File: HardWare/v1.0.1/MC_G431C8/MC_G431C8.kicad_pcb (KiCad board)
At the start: 2 copper layers, 154 parts, among them J1 Conn_01x02, J2 Conn_01x03, J3 Conn_01x04, J4 Conn_01x06, J5 Conn_01x03, Q1 MMBT3904L, U1 STM32G431C8, U2 fd6288t, U3 LMV324I, U4 TL431DBZ, U5 SGM6232YPS8G, U6 AMS1117-3.3, U7 AMS1117-5.0, U8 AS5047D, Y1 32MHZ

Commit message: 20240605 01:28 完成硬件初步布局
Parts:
- C12, C13, C26, C27, C28, C29, C30, C31, C5, C6, C8, C9, D10, D11, D12, D13, D4, D8, D9, R19, R2, R20, R21, R22, R24, R25, R26, R27, R30, R31, R32, R33, R7, TP1, TP10, TP11, TP12, TP13, TP14, TP15, TP16, TP17, TP18, TP19, TP2, TP4, TP5, TP6, TP7, TP8, TP9: moved to B.Cu
- moved U3 151.7 mm to (167.6, 105.4)
- moved U8 148.9 mm to (188.0, 85.1)
- moved Q8 126.9 mm to (165.4, 80.8), turned to 90 degrees
- moved Q6 122.0 mm to (158.7, 80.8), turned to 90 degrees
- moved R29 119.1 mm to (176.5, 108.0), turned to 180 degrees
- moved C36 115.9 mm to (166.6, 95.4)
- moved C37 115.9 mm to (166.6, 97.9)
- moved C38 115.9 mm to (166.6, 100.4)
- moved R35 115.9 mm to (174.6, 97.9)
- moved R36 115.9 mm to (174.6, 100.4)
- moved R37 115.9 mm to (174.6, 102.9)
- moved R38 115.9 mm to (174.6, 105.4)
- moved R42 115.9 mm to (178.6, 95.4)
- moved R43 115.9 mm to (178.6, 97.9)
- moved R44 115.9 mm to (178.6, 100.4)
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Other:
- board outline added: 100 x 50 mm

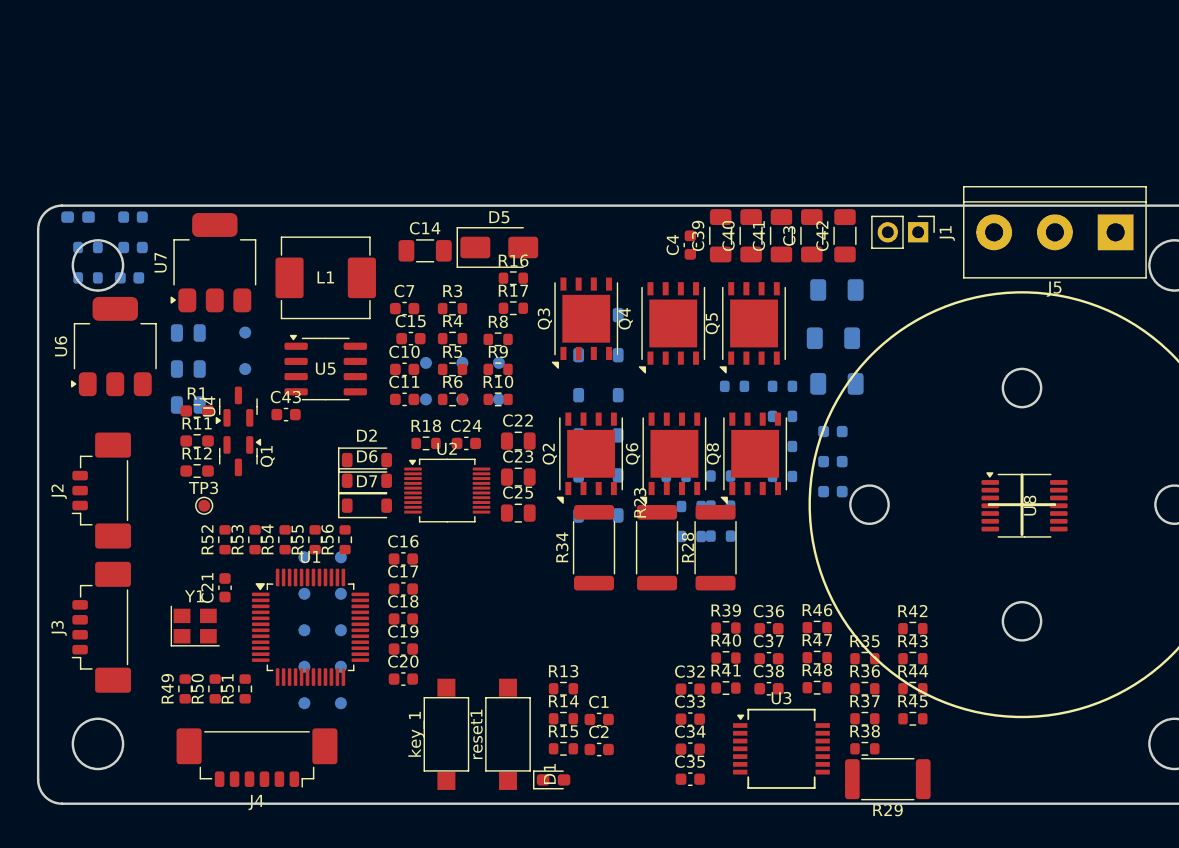
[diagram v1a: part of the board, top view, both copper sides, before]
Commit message: 20240606 01:01 硬件:电源布局完成
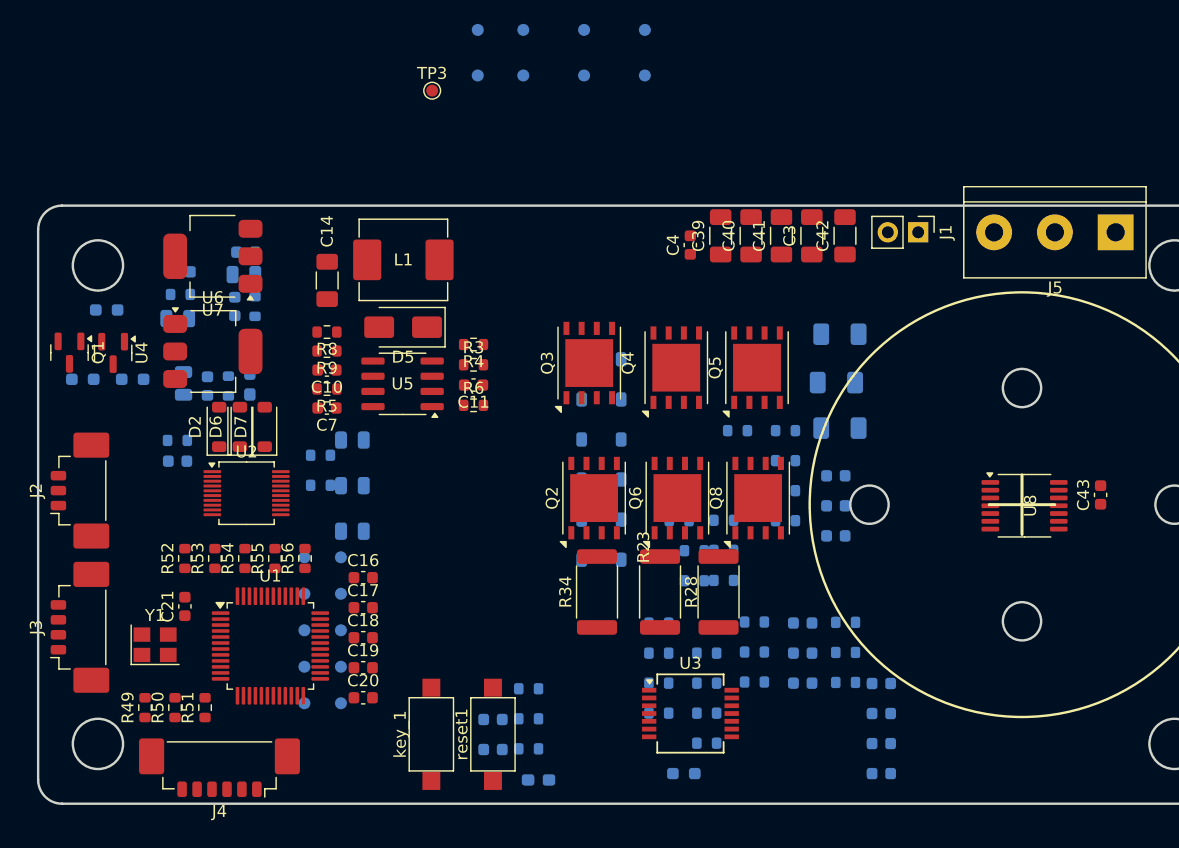
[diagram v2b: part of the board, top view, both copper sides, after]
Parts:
- C1, C15, C2, C22, C23, C24, C25, C32, C33, C34, C35, C36, C37, C38, D1, R1, R10, R11, R12, R13, R14, R15, R16, R17, R18, R35, R36, R37, R38, R39, R40, R41, R42, R43, R44, R45, R46, R47, R48: moved to B.Cu
- R29: footprint Resistor_SMD:R_2512_6332Metric -> Resistor_SMD:R_0603_1608Metric_Pad0.98x0.95mm_HandSolder; moved to B.Cu
- moved C43 68.4 mm to (194.3, 84.2), turned to 90 degrees
- moved TP3 39.6 mm to (138.4, 50.4)
- moved TP2 34.4 mm to (142.2, 45.3)
- moved TP16 31.7 mm to (156.2, 45.3)
- moved TP15 29.7 mm to (156.2, 49.1)
- moved TP18 29.0 mm to (146.1, 45.3)
- moved TP1 29.0 mm to (142.2, 49.1)
- moved TP17 28.9 mm to (151.1, 49.1)
- moved TP14 28.7 mm to (151.1, 45.3)
- moved TP19 28.3 mm to (146.1, 49.1)
- moved C24 24.2 mm to (117.2, 81.4), turned to 180 degrees
- moved R16 21.9 mm to (129.1, 80.9), turned to 180 degrees
- moved R17 21.9 mm to (129.1, 83.4), turned to 180 degrees
- moved R10 21.8 mm to (123.6, 68.4), turned to 90 degrees
- moved R42 21.2 mm to (157.4, 94.9), turned to 180 degrees
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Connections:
- TP11 pad 1: /TIM1_CH1N -> unconnected-(TP11-Pad1)

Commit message: 20240607 01:44 硬件初步布局已完成
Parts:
- C16, C17, C18, C19, R49, R50, R51, R52, R53, R54, R55, R56, TP3: moved to B.Cu
- R21, R22, R26, R27, R32, R33: moved to F.Cu
- moved TP18 82.6 mm to (69.4, 76.0)
- moved TP19 82.6 mm to (69.4, 79.9)
- moved TP1 82.6 mm to (65.5, 79.9)
- moved TP15 82.6 mm to (79.5, 79.9)
- moved TP16 82.6 mm to (79.5, 76.0)
- moved TP2 82.6 mm to (65.5, 76.0)
- moved TP14 82.6 mm to (74.4, 76.0)
- moved TP17 82.6 mm to (74.4, 79.9)
- moved TP3 64.2 mm to (81.5, 80.1), turned to 180 degrees
- moved TP4 47.6 mm to (85.1, 76.0), turned to -90 degrees
- moved TP5 45.7 mm to (88.1, 76.0), turned to -90 degrees
- moved TP6 44.1 mm to (91.2, 76.0), turned to -90 degrees
- moved TP9 43.9 mm to (85.1, 79.1), turned to -90 degrees
- moved TP7 42.9 mm to (94.2, 76.0), turned to -90 degrees
- moved C34 42.6 mm to (133.4, 103.7), turned to 90 degrees
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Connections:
- C20 pad 2: Net-(C20-Pad2) -> GND
- C21 pad 2: Net-(C20-Pad2) -> GND
- R51 pad 1: /SPI1_CS -> /SPI1_MOSI
- R52 pad 1: /SPI1_MOSI -> /SPI1_MISO
- R53 pad 1: /SPI1_MISO -> /SPI1_CLK
- R54 pad 1: /SPI1_CLK -> /SPI1_CS

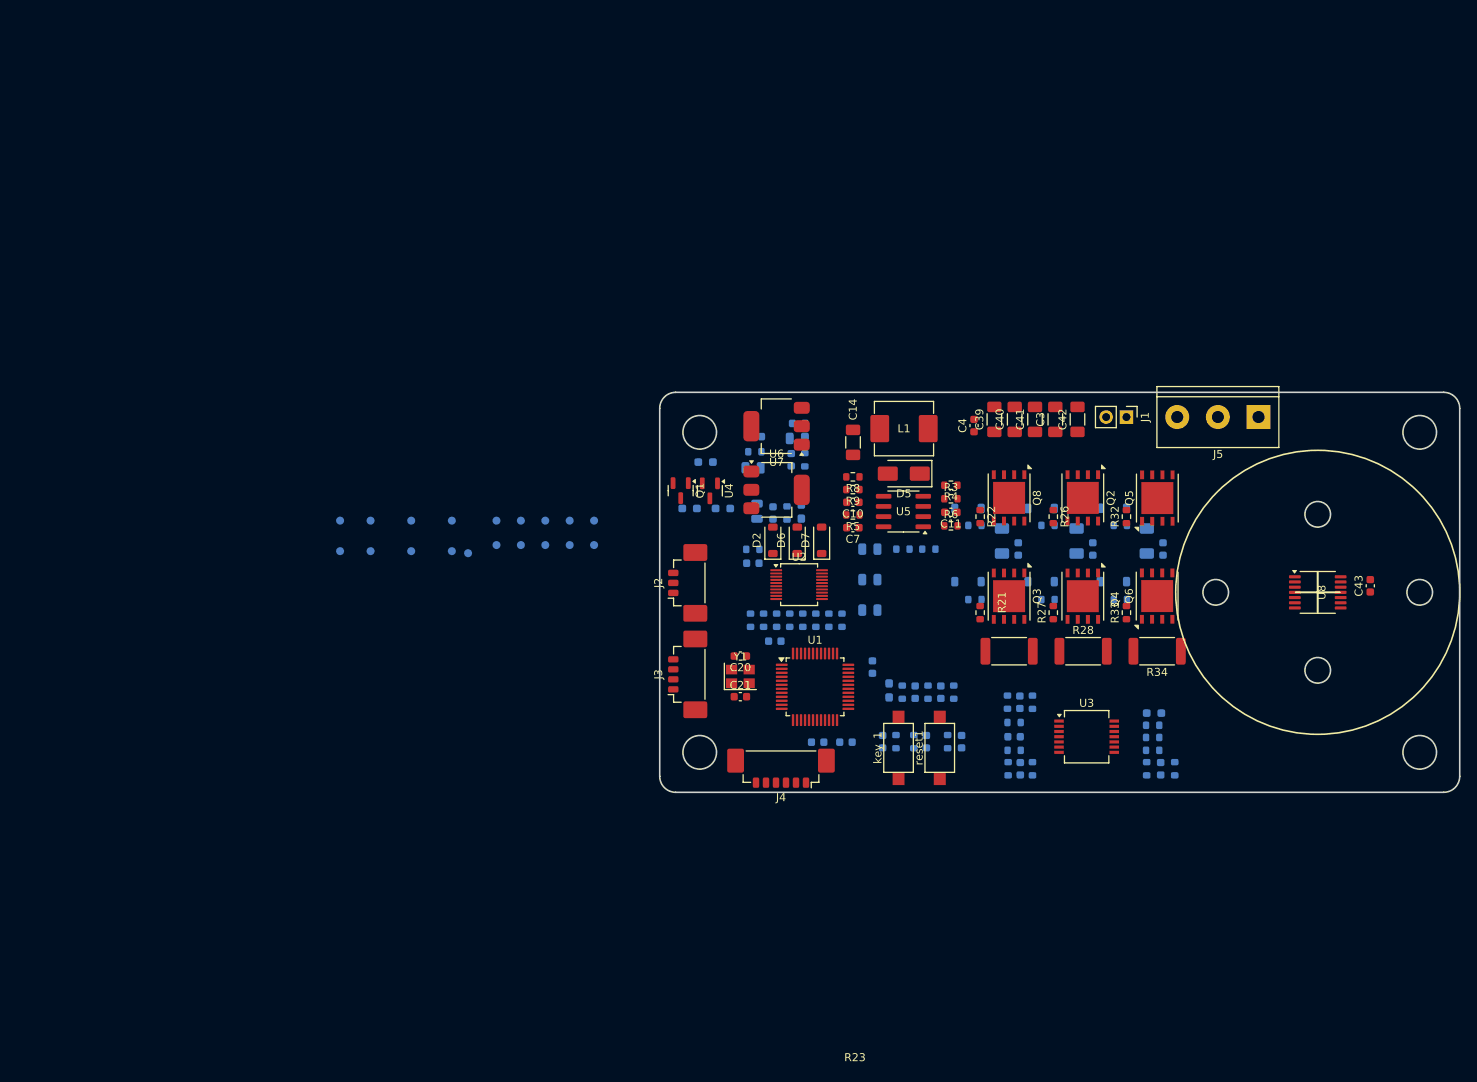
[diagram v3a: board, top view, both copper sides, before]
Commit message: 20240608 增加Can电路，优化整体布局
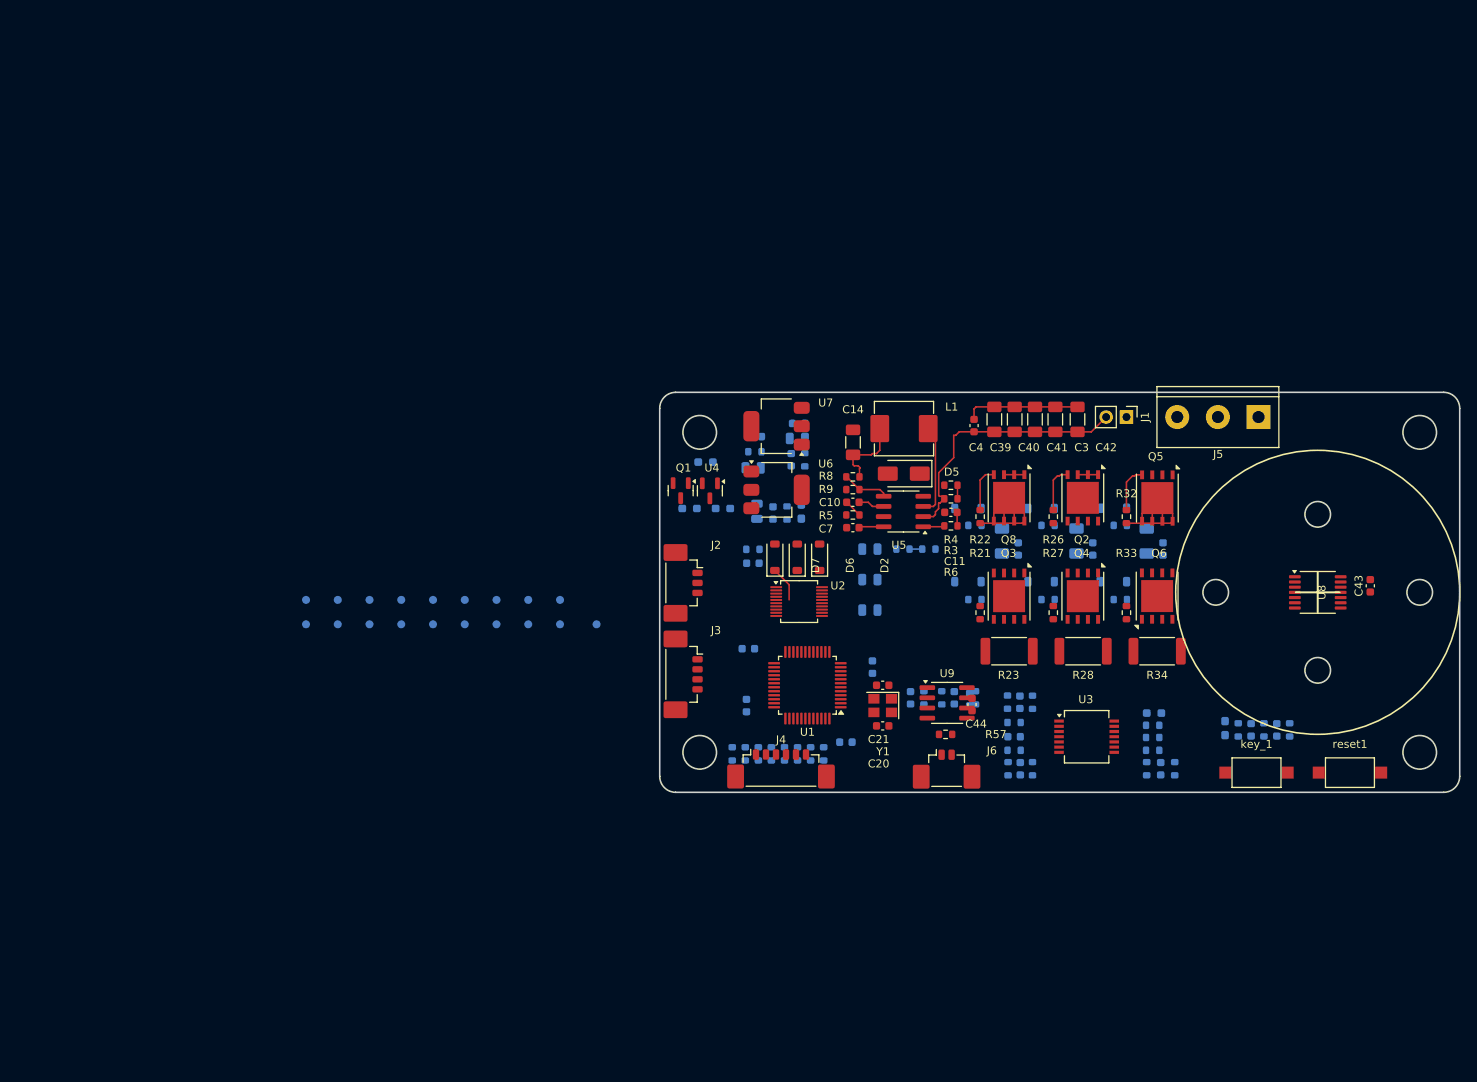
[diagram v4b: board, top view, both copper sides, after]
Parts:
- added C44: 0.1uF, Capacitor_SMD:C_0603_1608Metric, F.Cu at (144.5, 99.0)
- added J6: Conn_01x02, Connector_Molex:Molex_PicoBlade_53398-0271_1x02-1MP_P1.25mm_Vertical, F.Cu at (141.4, 106.5)
- added R57: 120R, Resistor_SMD:R_0603_1608Metric, F.Cu at (141.2, 102.8)
- added U9: TJA1042T-3, Package_SO:SOIC-8_3.9x4.9mm_P1.27mm, F.Cu at (141.4, 98.8)
- moved reset1 51.4 mm to (191.8, 107.5), turned to 180 degrees
- moved key_1 44.8 mm to (180.1, 107.5), turned to 180 degrees
- moved C1 42.3 mm to (179.4, 102.2)
- moved C2 42.3 mm to (182.6, 102.2)
- moved D1 42.3 mm to (176.2, 102.0)
- moved R14 42.3 mm to (184.2, 102.2)
- moved R15 42.3 mm to (177.8, 102.2)
- moved R13 42.3 mm to (181.0, 102.2)
- moved TP15 20.3 mm to (97.6, 89.0)
- moved C20 19.8 mm to (133.4, 101.7), turned to 0 degrees
- moved Y1 18.2 mm to (133.4, 99.2), turned to 180 degrees
- moved C21 17.9 mm to (133.4, 96.6), turned to 180 degrees
- moved R49 16.9 mm to (114.6, 105.2)
- moved R50 16.9 mm to (116.2, 105.2)
- moved R51 16.9 mm to (117.8, 105.2)
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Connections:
- TP11 pad 1: unconnected-(TP11-Pad1) -> /TIM1_CH1N
- U1 pad 26: unconnected-(U1-PB12-Pad26) -> /KEY_01
- U1 pad 33: /KEY_01 -> /CAN_RX
- U1 pad 34: unconnected-(U1-PA12-Pad34) -> /CAN_TX
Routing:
- net +24V: track 0.00 -> 38.4 mm
- net /Driver/W: track 0.00 -> 19.6 mm
- net /Driver/U: track 0.00 -> 19.3 mm
- net GND: track 0.04 -> 14.4 mm
- net Net-(U5-SW): track 0.00 -> 11.5 mm
- net Net-(C14-Pad1): track 0.00 -> 9.76 mm
- net Net-(U5-FB): track 0.00 -> 5.90 mm
- net Net-(D12-A): track 0.00 -> 5.82 mm
- net Net-(D10-A): track 0.00 -> 5.81 mm
- net Net-(D9-A): track 0.00 -> 5.74 mm
- net Net-(D7-K): track 0.00 -> 4.42 mm
- net Net-(U5-COMP): track 0.00 -> 3.29 mm
- net Net-(U5-SS): track 0.00 -> 3.12 mm
- net Net-(U5-BS): track 0.00 -> 2.68 mm
- net Net-(C10-Pad2): track 0.00 -> 2.26 mm
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
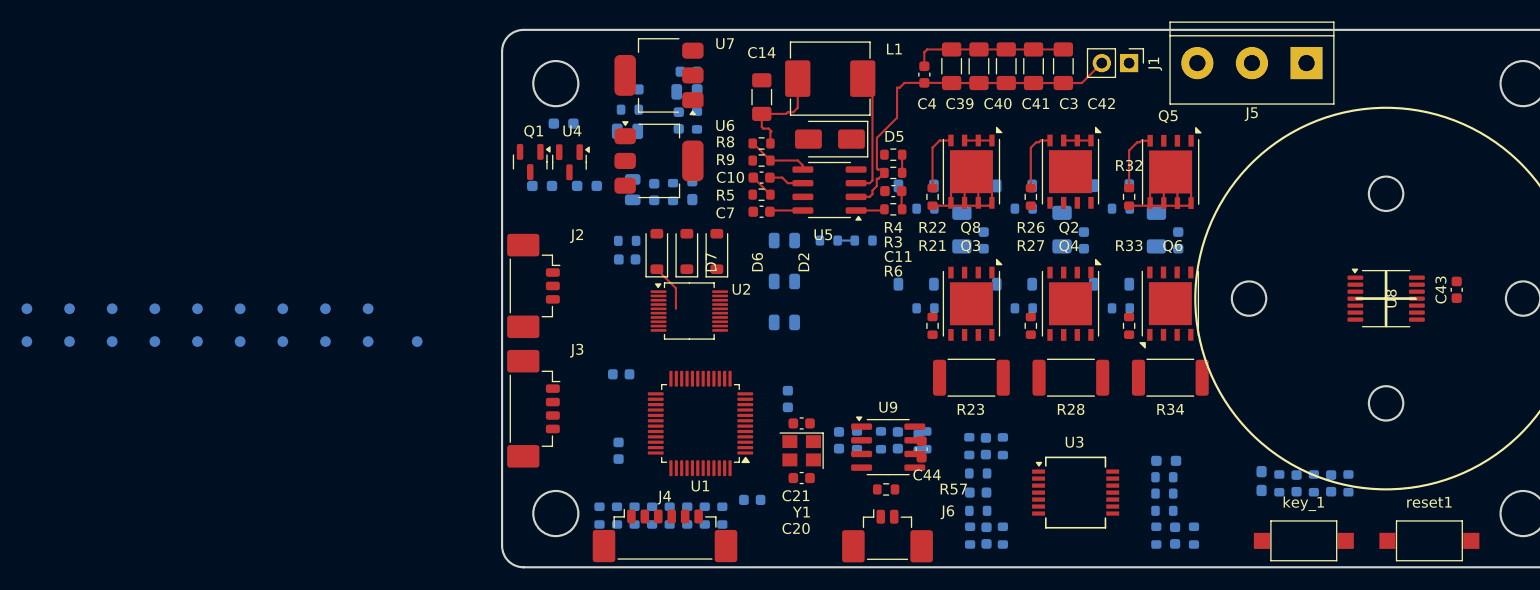
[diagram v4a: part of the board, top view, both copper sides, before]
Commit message: 20240610 硬件布局完成95%，软件增加速度环
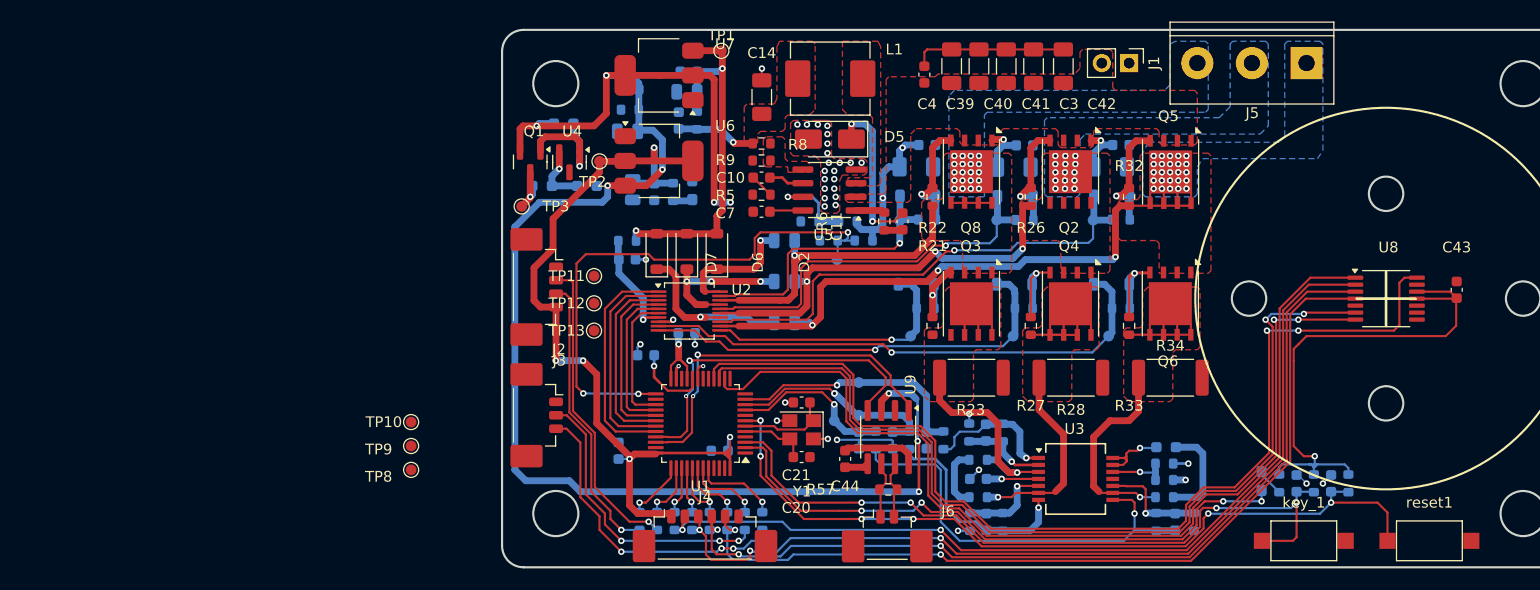
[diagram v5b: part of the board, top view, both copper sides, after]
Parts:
- R3, R4: moved to B.Cu
- TP1, TP10, TP11, TP12, TP13, TP2, TP3, TP8, TP9: moved to F.Cu
- moved TP19 96.7 mm to (161.9, 88.5)
- moved TP18 87.8 mm to (153.0, 88.5)
- moved TP16 87.7 mm to (160.5, 77.7)
- moved TP17 74.3 mm to (143.5, 88.5)
- moved TP14 73.7 mm to (142.5, 77.7)
- moved TP1 70.0 mm to (125.9, 62.0), turned to 0 degrees
- moved TP4 59.7 mm to (136.7, 81.4)
- moved TP5 56.2 mm to (136.4, 96.4)
- moved TP15 55.1 mm to (151.5, 77.7)
- moved TP2 55.0 mm to (114.6, 72.2), turned to 0 degrees
- moved TP6 54.5 mm to (138.7, 95.9)
- moved TP7 50.1 mm to (138.7, 92.8)
- moved TP3 36.4 mm to (107.3, 76.4), turned to 0 degrees
- moved TP11 29.6 mm to (114.1, 82.9)
- moved TP12 25.2 mm to (114.1, 85.4)
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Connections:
- net /CAN_H renamed /CAN_N
- net /CAN_L renamed /CAN_P
- net /CAN_RX renamed /CAN_+
- net /CAN_TX renamed /CAN_-
- C22 pad 2: /Driver/V -> Net-(D2-K)
- C36 pad 2: /OP_I_V -> /OP_I_W
- C38 pad 2: /OP_I_W -> /OP_I_V
- D2 pad 1: /Driver/V -> Net-(D2-K)
- J3 pad 2: /SWDIO -> /SWCLK
- J3 pad 3: /SWCLK -> /SWDIO
- J4 pad 2: /SPI1_CLK -> /SPI1_CS
- J4 pad 3: /SPI1_MISO -> /SPI1_CLK
- J4 pad 4: /SPI1_MOSI -> /SPI1_MISO
- J4 pad 5: /SPI1_CS -> /SPI1_MOSI
- R40 pad 2: /Driver/i_v -> /Driver/i_w
- R44 pad 2: /OP_I_V -> /OP_I_W
- R46 pad 2: /Driver/i_w -> /Driver/i_v
- R48 pad 2: /OP_I_W -> /OP_I_V
- U1 pad 26: /KEY_01 -> unconnected-(U1-PB12-Pad26)
- U1 pad 3: unconnected-(U1-PC14-Pad3) -> /KEY_01
- U2 pad 20: /Driver/V -> Net-(D2-K)
- U3 pad 6: /Driver/i_w -> /Driver/i_v
- U3 pad 9: /Driver/i_v -> /Driver/i_w
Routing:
- net +3V3: track 0.00 -> 143.8 mm, vias 0 -> 9
- net +5V: track 0.00 -> 143.3 mm, vias 0 -> 9
- net /ENCODER_Z: track 0.00 -> 97.8 mm, vias 0 -> 2
- net /ENCODER_B: track 0.00 -> 89.1 mm, vias 0 -> 2
- net /ENCODER_A: track 0.00 -> 88.6 mm, vias 0 -> 2
- net /SPI1_CLK: track 0.00 -> 85.5 mm, vias 0 -> 3
- net /SPI1_CS: track 0.00 -> 84.9 mm, vias 0 -> 2
- net /SPI1_MISO: track 0.00 -> 84.8 mm, vias 0 -> 3
- net /SPI1_MOSI: track 0.00 -> 82.2 mm, vias 0 -> 2
- net /RST: track 0.00 -> 75.5 mm, vias 0 -> 6
- net /KEY_01: track 0.00 -> 68.2 mm, vias 0 -> 4
- net /LED_01: track 0.00 -> 57.1 mm, vias 0 -> 4
- net /Driver/W_CHN: track 0.00 -> 49.8 mm, vias 0 -> 1
- net /ADC_VBUS: track 1.59 -> 51.1 mm, vias 0 -> 3
- net /Driver/W: track 19.6 -> 68.5 mm, vias 0 -> 28
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- added copper zone on F.Cu, net +24V
- added copper zone on B.Cu, net /Driver/U
- added copper zone on F.Cu, net /Driver/U
- added copper zone on B.Cu, net /Driver/V
- added copper zone on F.Cu, net /Driver/V
- added copper zone on B.Cu, net /Driver/W
- added copper zone on F.Cu, net /Driver/W
- added copper zone on F.Cu, net /Driver/i_u
- added copper zone on F.Cu, net /Driver/i_v
- added copper zone on F.Cu, net /Driver/i_w
- added copper zone on F.Cu, net GND
- added copper zone on F.Cu, net Net-(C14-Pad1)
- added copper zone on F.Cu, net Net-(U5-FB)
- added copper zone on F.Cu, net Net-(U5-SW)
